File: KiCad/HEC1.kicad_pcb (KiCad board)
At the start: 2 copper layers, 243.8 x 170.2 mm, 654 parts, among them J1 Barrel_Jack_Switch, J2 Conn_02x12_Odd_Even, J3 Conn_02x05_Odd_Even, J5 Screw_Terminal_01x02, J6 DE9_Plug_MountingHoles, J7 AudioJack3, J8 NES_Port_Male, J9 Conn_02x14_Odd_Even, SW1 SW_DIP_x04, SW2 SW_Push, U1 Z80CPU, U10 74LS32, U11 74LS00, U12 74LS04, U13 74LS245, U14 74LS245, U15 74LS32, U16 74LS32, U17 74LS20, U18 74LS138, U19 74LS30, U2 AS6C4008-55PCN, U20 74LS574, U21 74LS574, U22 74LS02, U23 74LS74, U24 74LS74, U25 74LS541, U26 74LS541, U27 74LS74, U28 74LS30, U29 74LS74, U3 AS6C4008-55PCN, U30 74LS74, U31 74LS32, U32 LM79M05_TO220, U33 74LS20, U34 74LS393, U35 74LS08, U36 74LS574, U37 74LS32, U38 74LS47, U39 74LS47, U4 CY7C199, U40 DA04-11EWA, U41 74LS02, U42 74LS06, U44 74LS541, U5 CY7C199, U6 74LS138, U7 28C256, U8 74LS138, U9 74LS574, X1 CXO_DIP8, Y1 Crystal

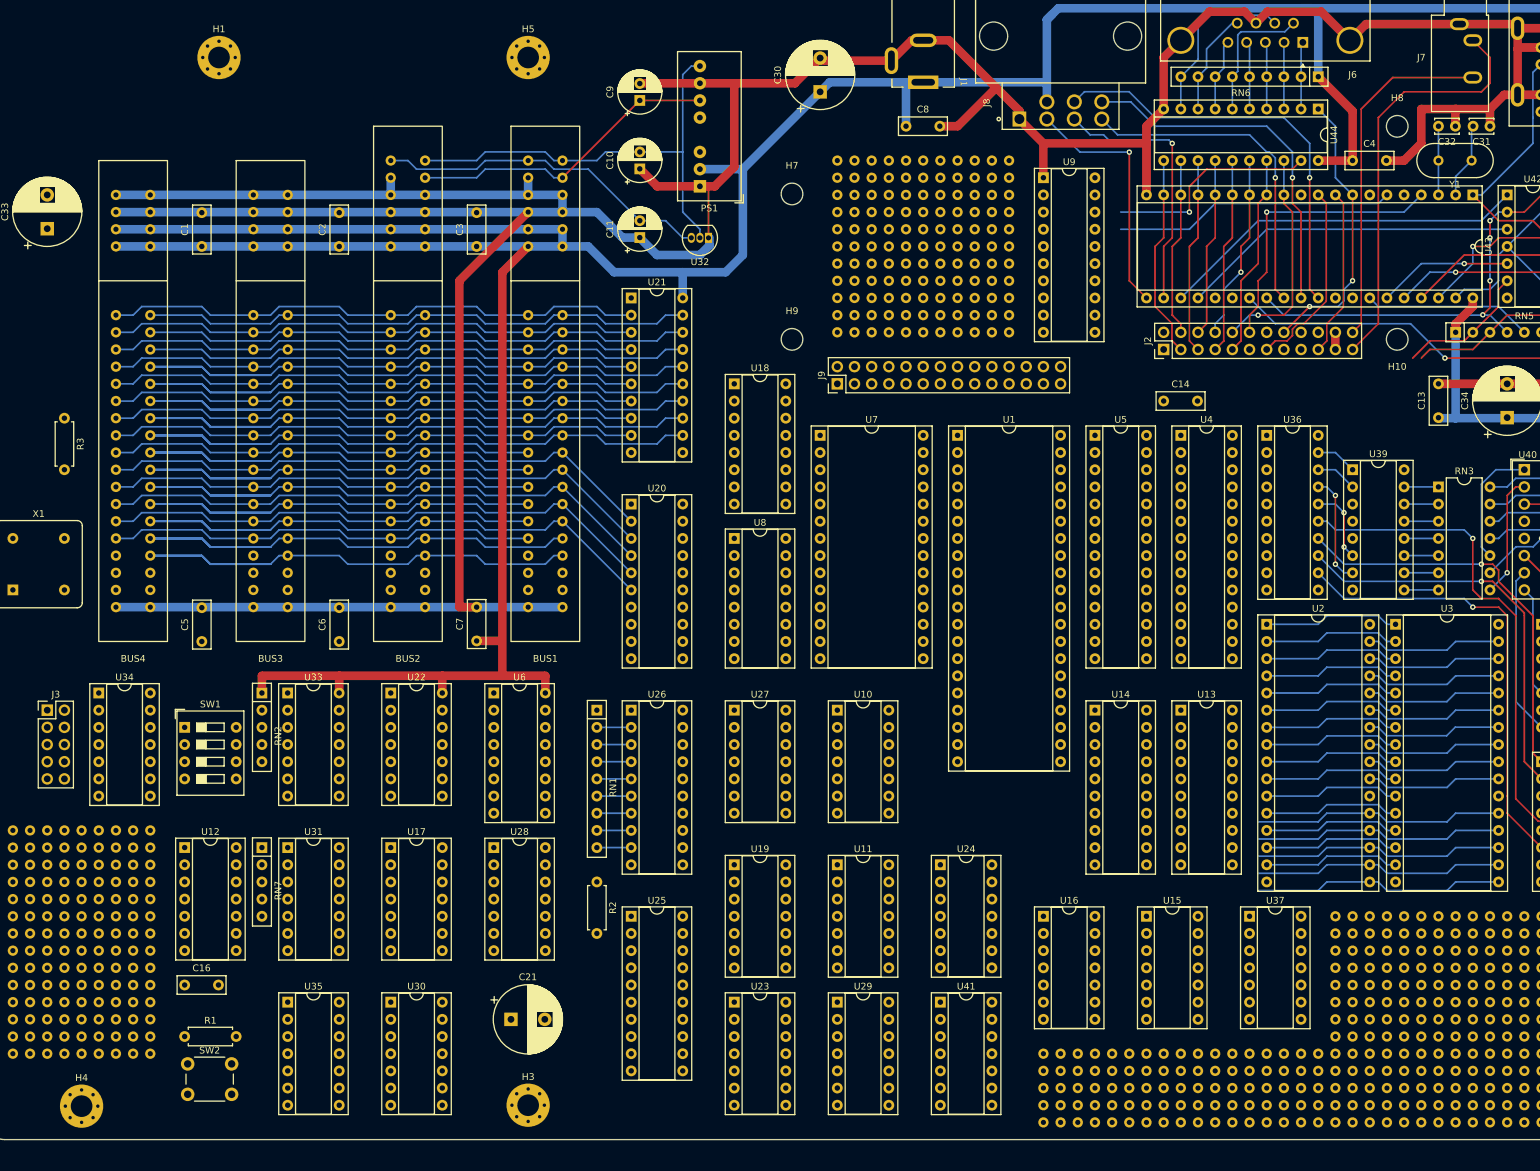
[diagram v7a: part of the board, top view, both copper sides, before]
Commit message: Livestream routing
First routing livestream! Routed a data bus and some traces protection and memory region.
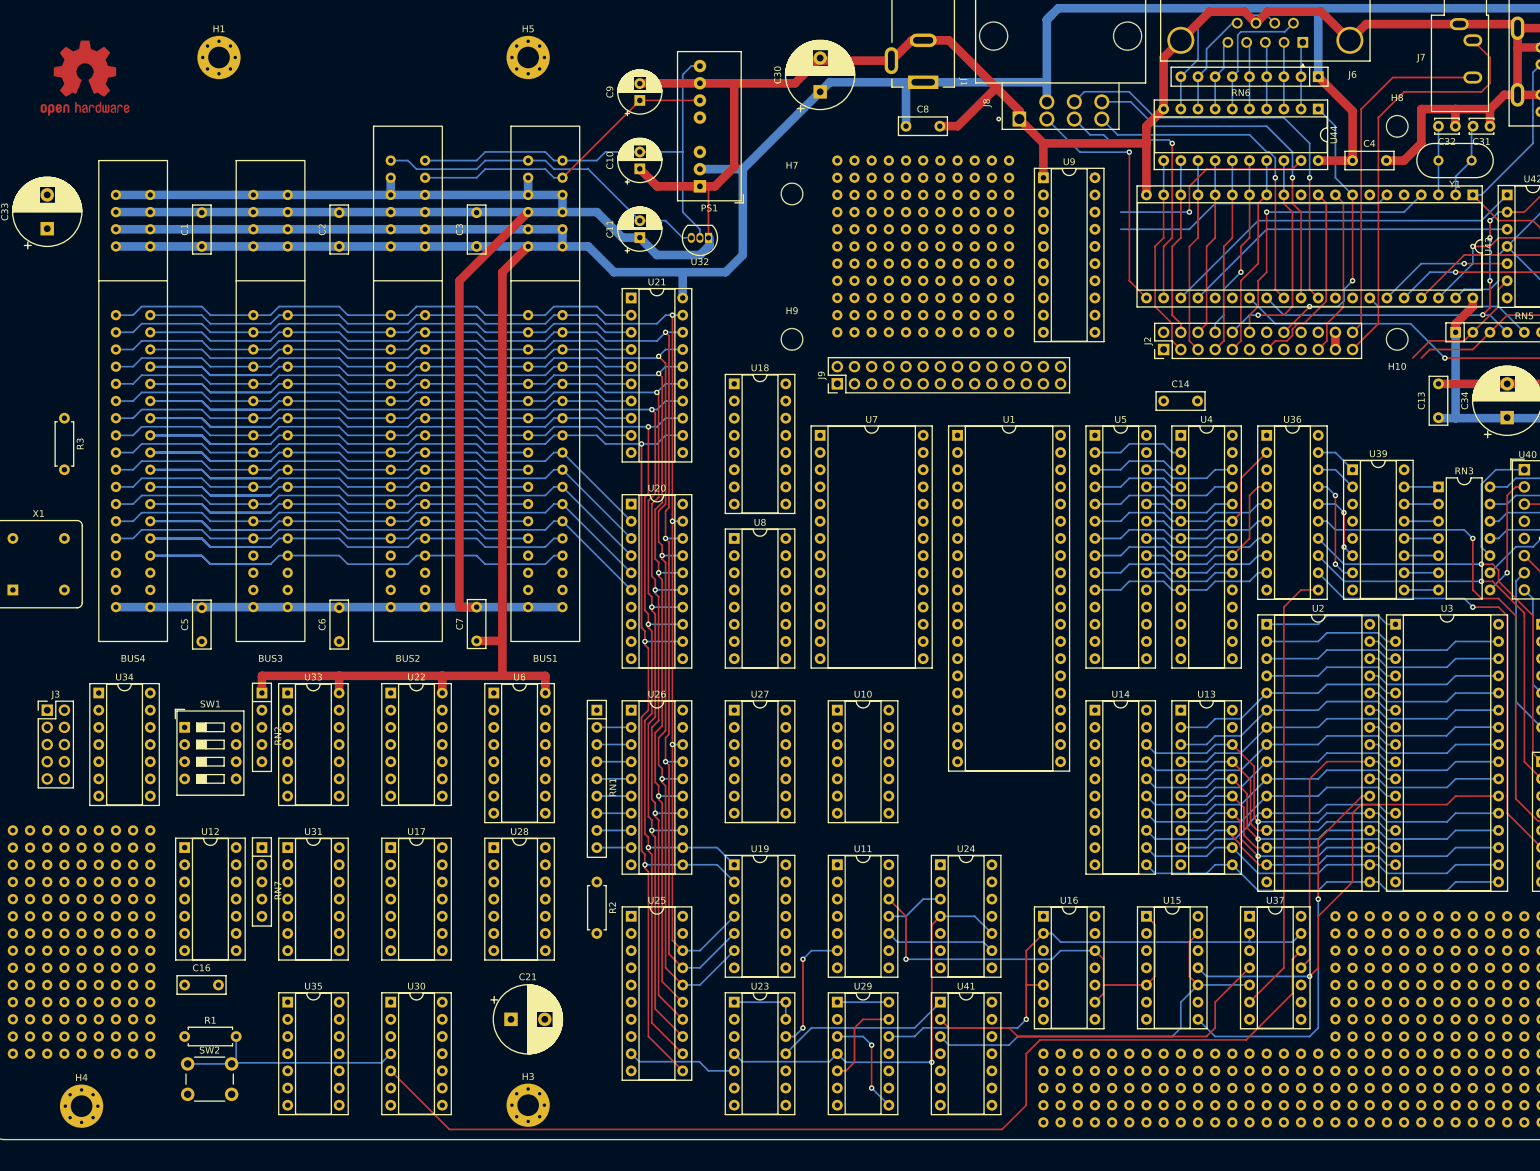
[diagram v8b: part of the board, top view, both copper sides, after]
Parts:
- added REF**: OSHW-Logo2_14.6x12mm_Copper, Symbol:OSHW-Logo2_14.6x12mm_Copper, F.Cu at (48.8, 38.6)
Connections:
- U11 pad 3: Net-(U23A-~{S}) -> Net-(U23B-~{S})
- U11 pad 6: Net-(U23A-D) -> Net-(U23B-D)
- U22 pad 13: Net-(U23B-C) -> Net-(U23A-C)
- U23 pad 10: /HEC_Protection/~{CLRINT} -> Net-(U23B-~{S})
- U23 pad 12: L -> Net-(U23B-D)
- U23 pad 2: Net-(U23A-D) -> L
- U23 pad 4: Net-(U23A-~{S}) -> /HEC_Protection/~{CLRINT}
- U23 pad 5: unconnected-(U23A-Q-Pad5) -> /HEC_Protection/~{IO_PROT}
- U23 pad 6: /HEC_CPU/~{NMI} -> unconnected-(U23A-~{Q}-Pad6)
- U23 pad 8: unconnected-(U23B-~{Q}-Pad8) -> /HEC_CPU/~{NMI}
- U23 pad 9: /HEC_Protection/~{IO_PROT} -> unconnected-(U23B-Q-Pad9)
- U41 pad 1: Net-(U23A-C) -> Net-(U23B-C)
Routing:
- net Net-(U30A-Q): track 0.00 -> 156.6 mm
- net /HEC_IO/D1: track 103.1 -> 240.5 mm, vias 0 -> 3
- net /HEC_IO/D2: track 120.1 -> 256.2 mm, vias 0 -> 4
- net /HEC_IO/D7: track 175.0 -> 310.1 mm, vias 0 -> 3
- net /HEC_IO/D0: track 120.1 -> 254.2 mm, vias 0 -> 4
- net /HEC_IO/D6: track 156.7 -> 290.7 mm, vias 0 -> 3
- net /HEC_IO/D3: track 121.4 -> 249.0 mm, vias 0 -> 3
- net /HEC_IO/D5: track 139.7 -> 266.7 mm, vias 0 -> 3
- net /HEC_IO/D4: track 138.4 -> 264.2 mm, vias 0 -> 4
- net /HEC_CPU/~{RD}: track 41.8 -> 119.9 mm, vias 2 -> 3
- net Net-(U36-Cp): track 0.00 -> 66.7 mm
- net /HEC_Memory/~{RAM1CS}: track 0.00 -> 66.4 mm, vias 0 -> 1
- net /HEC_CPU/~{WR}: track 129.3 -> 193.9 mm, vias 0 -> 1
- net /HEC_Protection/~{CLRINT}: track 0.00 -> 61.5 mm, vias 0 -> 1
- net /HEC_CPU/~{MREQ}: track 0.00 -> 60.8 mm
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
